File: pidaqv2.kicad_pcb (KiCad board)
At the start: 2 copper layers, 71.1 x 59.9 mm, 28 parts, among them J101 Screw_Terminal_01x10, J102 Screw_Terminal_01x06, J103 Conn_01x02_Male, J104 Screw_Terminal_01x04, J105 Screw_Terminal_01x08, U1 RASPBERRY_PI_3_MODEL_B+, U201 ADS1261BIRHBR, U301 ADS1261BIRHBR, U401 AD8426ACPZ-R7

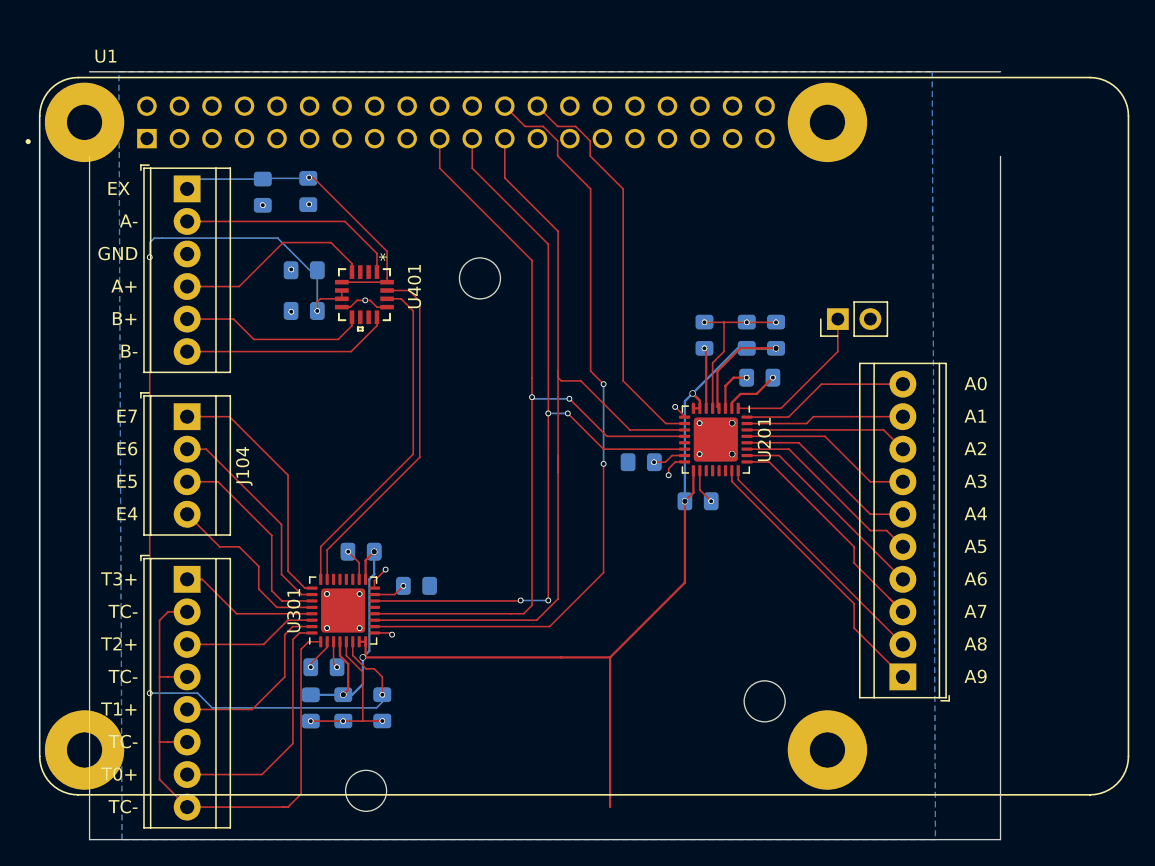
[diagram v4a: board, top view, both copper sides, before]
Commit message: slid the header to the right, and set IO to 3.3V
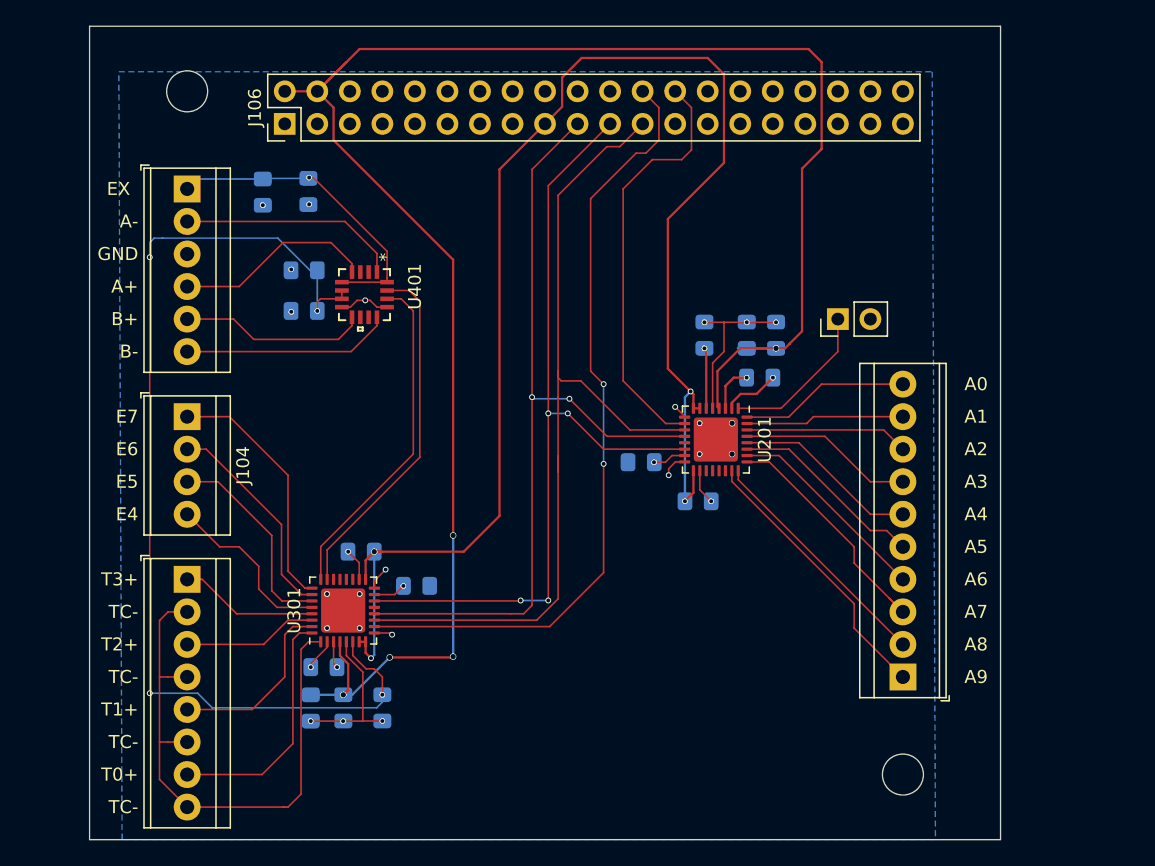
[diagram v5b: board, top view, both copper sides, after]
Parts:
- removed H104: MountingHole, MountingHole:MountingHole_3.2mm_M3_ISO7380
- removed U1: RASPBERRY_PI_3_MODEL_B+, RASPBERRY_PI_3_MODEL_B_:MODULE_RASPBERRY_PI_3_MODEL_B+
- added J106: Raspberry_Pi_2_3, Connector_PinHeader_2.54mm:PinHeader_2x20_P2.54mm_Vertical, F.Cu at (119.4, 68.6)
- moved H103 56.4 mm to (111.8, 66.0)
- moved H102 12.2 mm to (167.6, 119.4)
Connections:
- C204 pad 1: +5V -> +3V3
- C304 pad 1: +5V -> +3V3
- U201 pad 13: Net-(U201-Pad13) -> (no net)
- U201 pad 17: +5V -> +3V3
- U201 pad 19: Net-(U201-Pad19) -> (no net)
- U201 pad 20: Net-(U201-Pad20) -> (no net)
- U201 pad 21: Net-(U201-Pad21) -> (no net)
- U201 pad 22: Net-(U201-Pad22) -> (no net)
- U201 pad 7: +5V -> +3V3
- U201 pad 8: +5V -> +3V3
- U301 pad 13: Net-(U301-Pad13) -> (no net)
- U301 pad 17: +5V -> +3V3
- U301 pad 19: Net-(U301-Pad19) -> (no net)
- U301 pad 20: Net-(U301-Pad20) -> (no net)
- U301 pad 21: Net-(U301-Pad21) -> (no net)
- U301 pad 22: Net-(U301-Pad22) -> (no net)
- U301 pad 7: +5V -> +3V3
- U301 pad 8: +5V -> +3V3
- U401 pad 10: Net-(U401-Pad10) -> (no net)
- U401 pad 11: Net-(U401-Pad11) -> (no net)
- U401 pad 2: Net-(U401-Pad2) -> (no net)
- U401 pad 3: Net-(U401-Pad3) -> (no net)
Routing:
- net +3V3: track 0.00 -> 115.7 mm, vias 0 -> 4
- net +5V: track 101.1 -> 148.5 mm, vias 6 -> 5
- net SCLK: track 66.0 -> 68.8 mm
- net ~CS1: track 31.2 -> 32.9 mm
- net ~CS0: track 60.1 -> 60.8 mm
- net MISO: track 64.0 -> 64.7 mm
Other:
- board size 71.1 x 59.9 mm -> 71.1 x 63.5 mm
